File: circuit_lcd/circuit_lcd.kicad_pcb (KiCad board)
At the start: 2 copper layers, 86 x 86 mm, 24 parts, among them J1 Conn_01x04, J2 Conn_01x01, J3 Conn_01x04, J4 Conn_01x04, J5 Conn_01x01, J6 Conn_01x01, J7 Conn_01x01, M1 Stepper_Motor_bipolar, U3 HT1621B, U5 VIM-878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

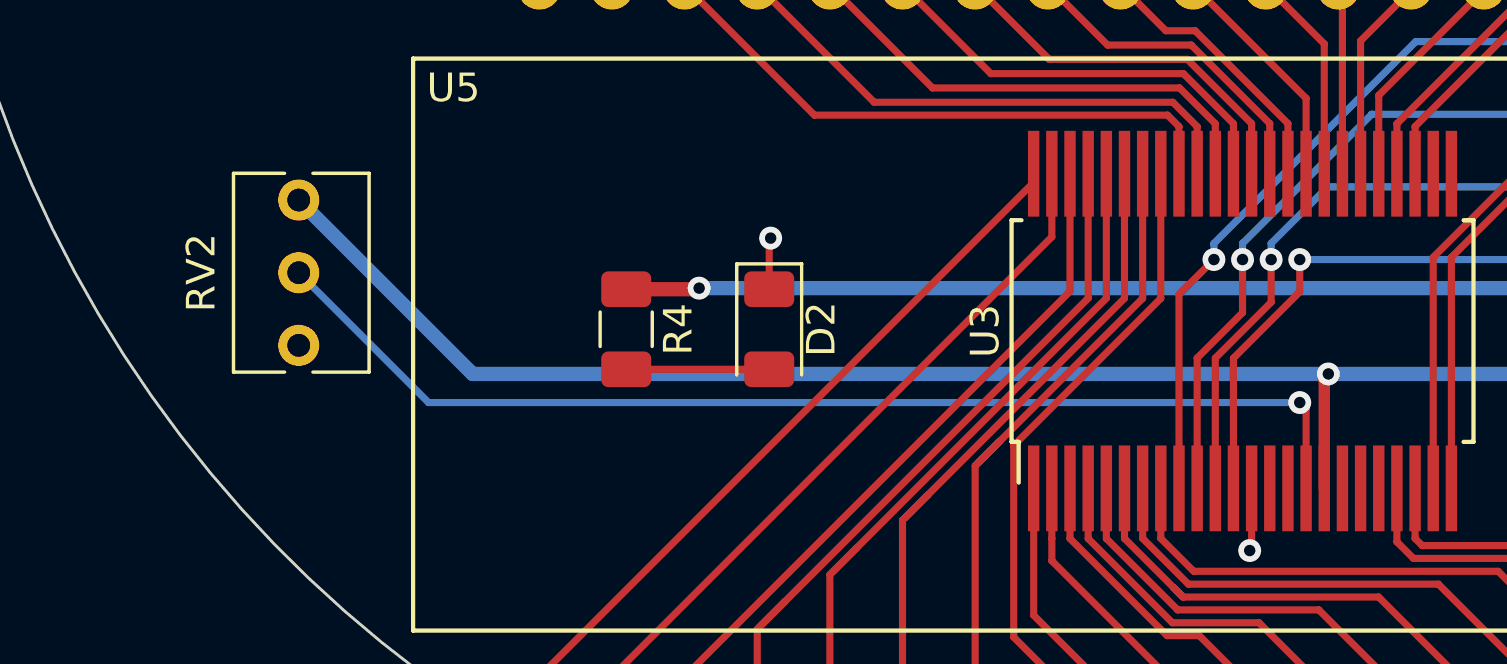
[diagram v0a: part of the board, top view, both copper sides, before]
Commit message: Removed contrast pot and renamed segment nets
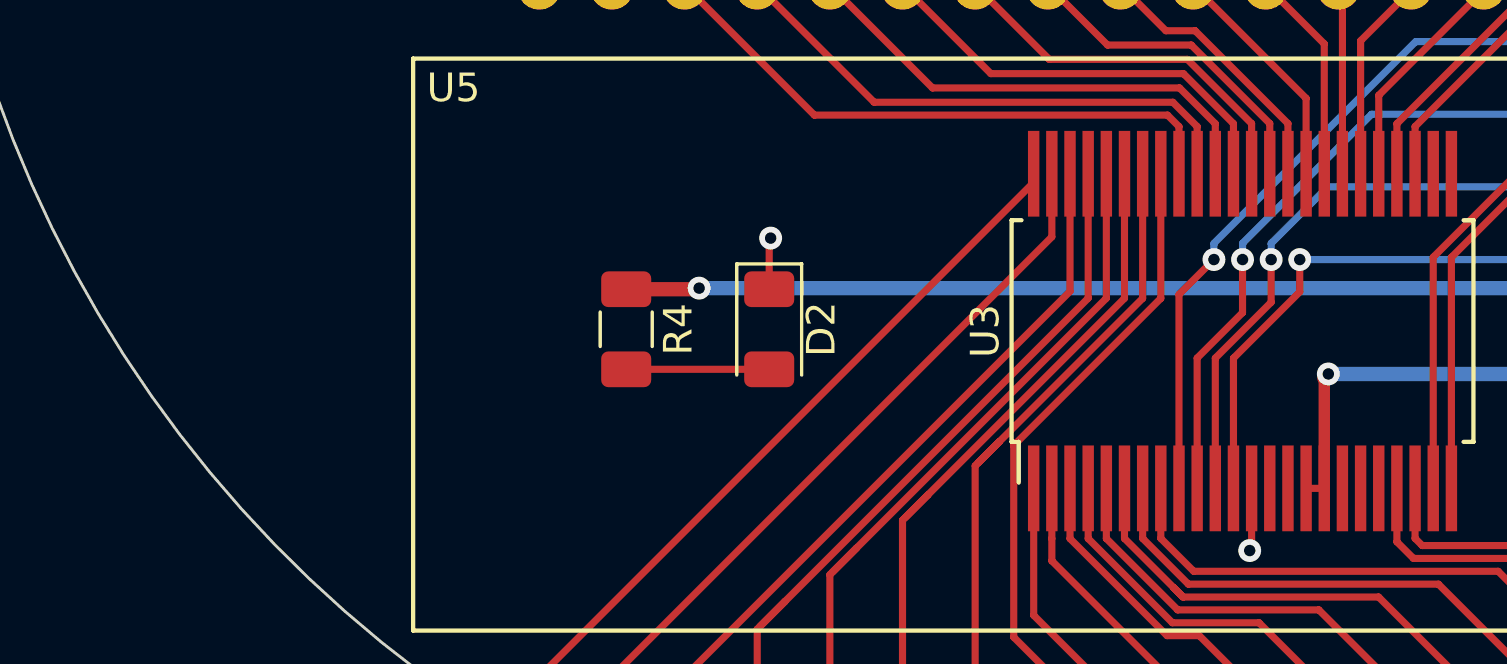
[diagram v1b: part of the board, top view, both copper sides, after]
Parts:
- removed RV2: R_POT, Potentiometer_THT:Potentiometer_Bourns_3266Y_Vertical
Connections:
- U3 pad 1: /SEG8 -> /SEG7
- U3 pad 16: Net-(RV2-Pad2) -> +5V
- U3 pad 2: /SEG9 -> /SEG6
- U3 pad 3: /SEG10 -> /SEG5
- U3 pad 4: /SEG11 -> /SEG4
- U3 pad 41: /SEG7 -> /SEG15
- U3 pad 42: /SEG6 -> /SEG14
- U3 pad 43: /SEG5 -> /SEG13
- U3 pad 44: /SEG4 -> /SEG12
- U3 pad 45: /SEG3 -> /SEG11
- U3 pad 46: /SEG2 -> /SEG10
- U3 pad 47: /SEG1 -> /SEG9
- U3 pad 48: /SEG0 -> /SEG8
- U3 pad 5: /SEG12 -> /SEG3
- U3 pad 6: /SEG13 -> /SEG2
- U3 pad 7: /SEG14 -> /SEG1
- U3 pad 8: /SEG15 -> /SEG0
- U5 pad 1: /SEG0 -> /SEG8
- U5 pad 10: /SEG9 -> /SEG6
- U5 pad 11: /SEG10 -> /SEG5
- U5 pad 12: /SEG11 -> /SEG4
- U5 pad 13: /SEG12 -> /SEG3
- U5 pad 14: /SEG13 -> /SEG2
- U5 pad 15: /SEG14 -> /SEG1
- U5 pad 16: /SEG15 -> /SEG0
- U5 pad 2: /SEG1 -> /SEG9
- U5 pad 3: /SEG2 -> /SEG10
- U5 pad 4: /SEG3 -> /SEG11
- U5 pad 5: /SEG4 -> /SEG12
- U5 pad 6: /SEG5 -> /SEG13
- U5 pad 7: /SEG6 -> /SEG14
- U5 pad 8: /SEG7 -> /SEG15
- U5 pad 9: /SEG8 -> /SEG7
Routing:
- net Net-(RV2-Pad2): track 40.0 -> 0.00 mm, vias 1 -> 0
- net +5V: track 165.1 -> 127.2 mm
- net /SEG8: track 8.73 -> 25.6 mm
- net /SEG9: track 9.53 -> 24.8 mm
- net /SEG10: track 11.0 -> 24.1 mm
- net /SEG6: track 22.0 -> 9.53 mm
- net /SEG7: track 21.1 -> 8.73 mm
- net /SEG5: track 22.8 -> 11.0 mm
- net /SEG11: track 12.9 -> 24.5 mm
- net /SEG4: track 23.7 -> 12.9 mm
- net /SEG3: track 24.5 -> 14.8 mm
- net /SEG12: track 14.8 -> 23.7 mm
- net /SEG2: track 24.1 -> 17.1 mm
- net /SEG1: track 24.8 -> 18.6 mm
- net /SEG13: track 17.1 -> 22.8 mm
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
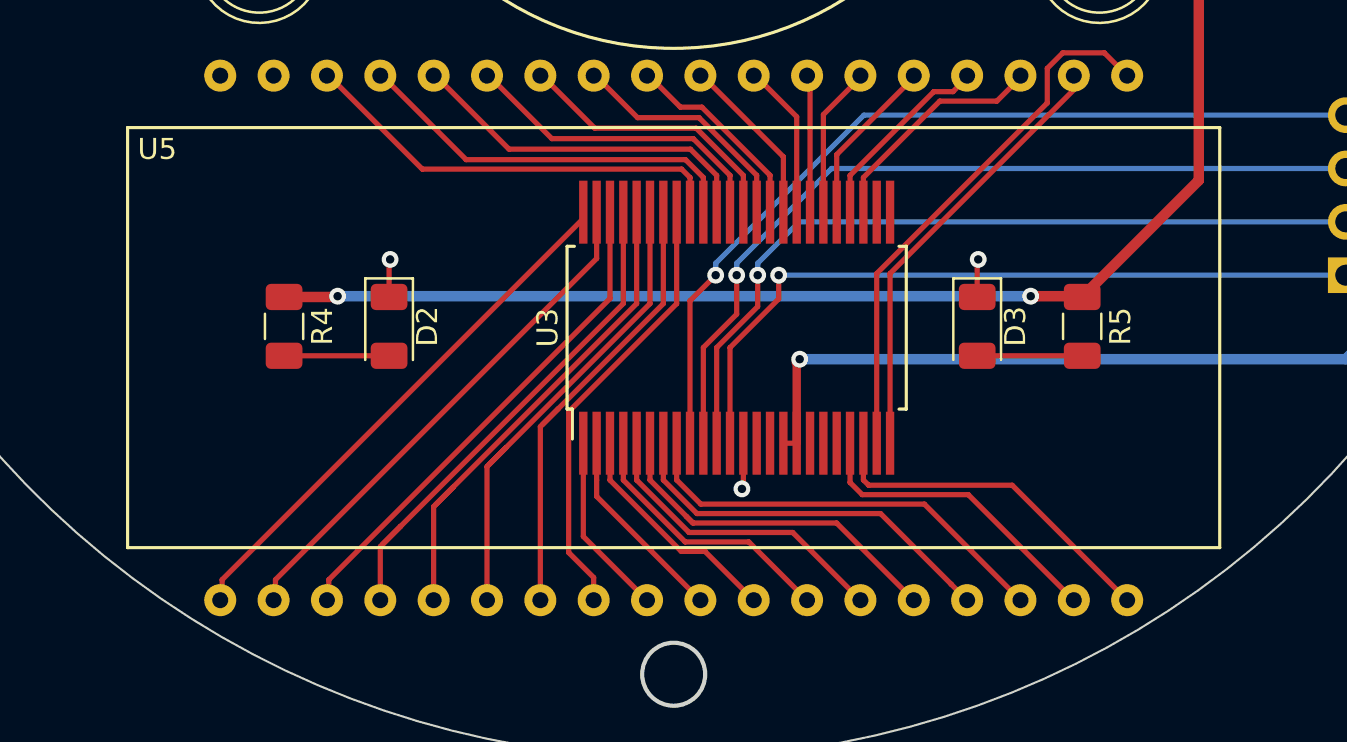
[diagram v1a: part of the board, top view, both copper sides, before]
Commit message: Fixed LCD footprint
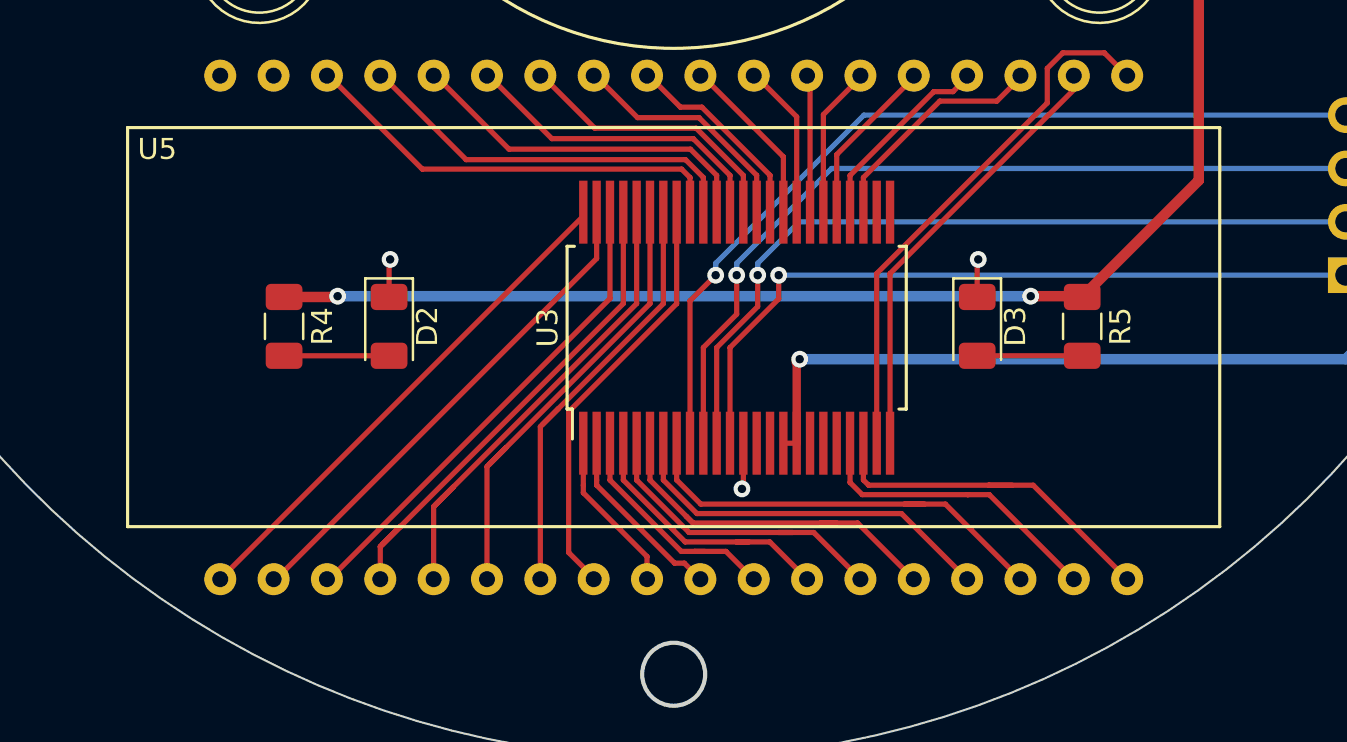
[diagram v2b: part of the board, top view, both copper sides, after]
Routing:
- net /SEG15: track 21.1 -> 20.0 mm
- net /SEG10: track 24.1 -> 23.0 mm
- net /SEG9: track 24.8 -> 23.8 mm
- net /SEG7: track 8.73 -> 7.73 mm
- net /SEG13: track 22.8 -> 21.8 mm
- net /SEG8: track 25.6 -> 24.6 mm
- net /SEG14: track 22.0 -> 21.0 mm
- net /SEG6: track 9.53 -> 8.80 mm
- net /COM1: track 16.7 -> 17.4 mm
- net /SEG0: track 20.5 -> 21.0 mm

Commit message: Added missing segments
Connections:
- U3 pad 25: (no net) -> /SEG31
- U3 pad 26: (no net) -> /SEG30
- U5 pad 21: /SEG29 -> /SEG31
- U5 pad 22: /SEG28 -> /SEG30
- U5 pad 23: /SEG27 -> /SEG29
- U5 pad 24: /SEG26 -> /SEG28
- U5 pad 25: /SEG25 -> /SEG27
- U5 pad 26: /SEG24 -> /SEG26
- U5 pad 27: /SEG23 -> /SEG25
- U5 pad 28: /SEG22 -> /SEG24
- U5 pad 29: /SEG21 -> /SEG23
- U5 pad 30: /SEG20 -> /SEG22
- U5 pad 31: /SEG19 -> /SEG21
- U5 pad 32: /SEG18 -> /SEG20
- U5 pad 33: /SEG17 -> /SEG19
- U5 pad 34: /SEG16 -> /SEG18
- U5 pad 35: (no net) -> /SEG17
- U5 pad 36: (no net) -> /SEG16
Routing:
- net /SEG31: track 0.00 -> 9.34 mm
- net /SEG30: track 0.00 -> 8.28 mm
- net /SEG20: track 13.3 -> 19.1 mm
- net /SEG16: track 20.9 -> 26.7 mm
- net /SEG19: track 15.2 -> 20.4 mm
- net /SEG21: track 11.4 -> 16.6 mm
- net /SEG18: track 17.1 -> 22.3 mm
- net /SEG17: track 19.0 -> 24.1 mm
- net /SEG22: track 9.49 -> 14.7 mm
- net /SEG23: track 8.10 -> 13.0 mm, vias 0 -> 1
- net /SEG24: track 7.31 -> 11.3 mm, vias 0 -> 1
- net /SEG29: track 11.2 -> 7.49 mm
- net /SEG25: track 6.52 -> 9.43 mm
- net /SEG28: track 9.38 -> 6.70 mm
- net /SEG27: track 8.06 -> 7.08 mm
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
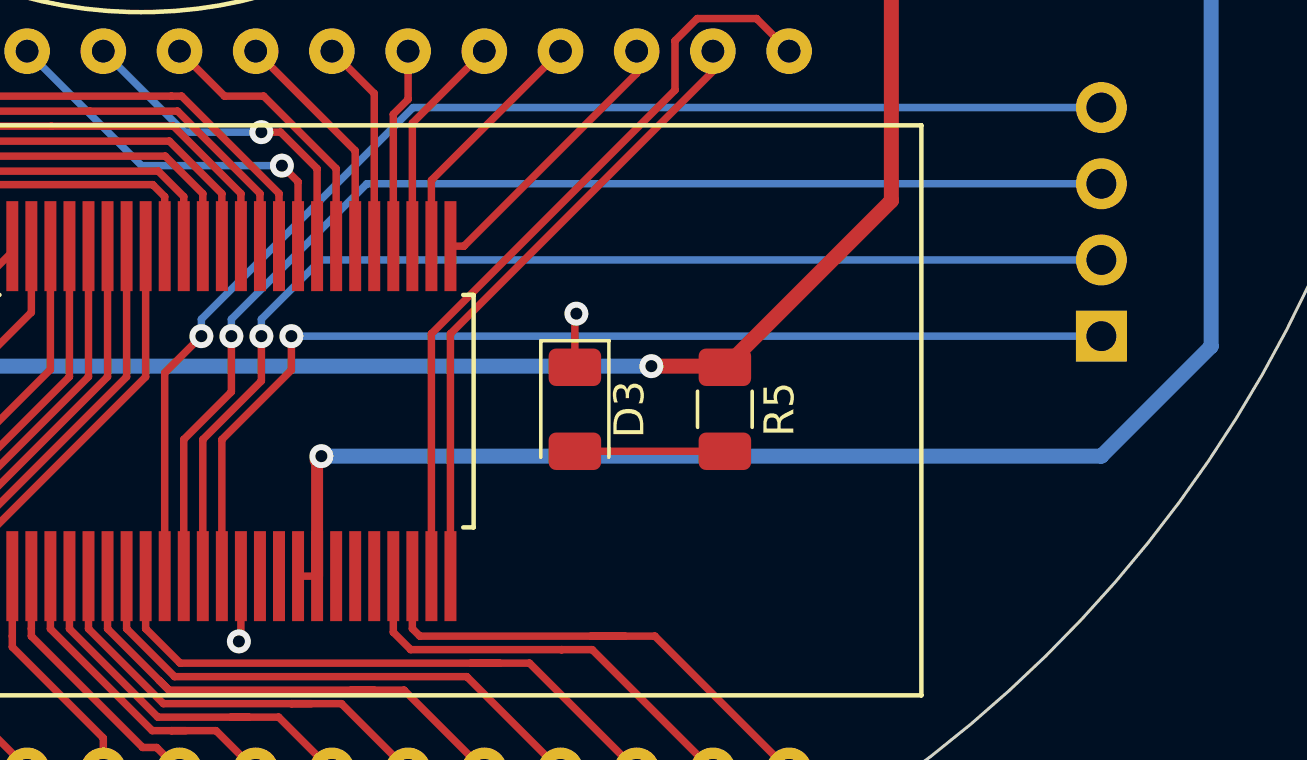
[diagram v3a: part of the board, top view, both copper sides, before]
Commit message: Removed unused LCD read net
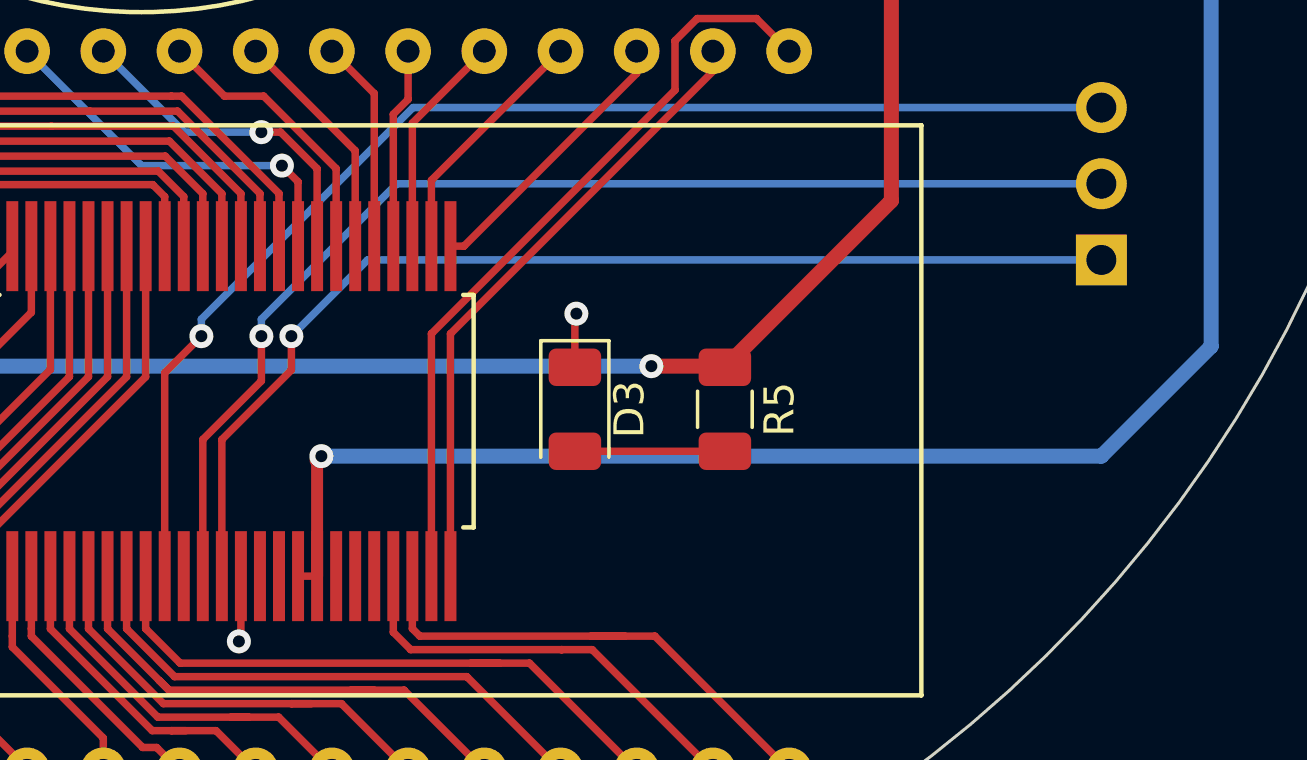
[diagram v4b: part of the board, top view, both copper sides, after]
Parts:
- J4: value Conn_01x04 -> Conn_01x03; footprint Connector_PinSocket_2.54mm:PinSocket_1x04_P2.54mm_Vertical -> Connector_PinSocket_2.54mm:PinSocket_1x03_P2.54mm_Vertical
- moved J4 2.54 mm to (182.0, 117.5)
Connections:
- J4 pad 3: /LCD_RD -> /LCD_CS
- U3 pad 10: /LCD_RD -> (no net)
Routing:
- net /LCD_RD: track 40.1 -> 0.00 mm, vias 1 -> 0
- net /LCD_DATA: track 36.0 -> 37.0 mm
- net /LCD_WR: track 38.2 -> 39.2 mm
